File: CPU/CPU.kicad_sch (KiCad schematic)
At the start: 219 parts, among them J1 Conn_02x36_Top_Bottom, P2 Conn_02x13_Top_Bottom, P3 Conn_02x13_Top_Bottom, P4 IDC-16, P5 Conn_02x25_Counter_Clockwise, P6 Conn_02x25_Counter_Clockwise, P7 Conn_02x07_Counter_Clockwise, P8 Conn_02x08_Odd_Even

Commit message: CPU: Fix a huuuge erratum
CPU-E001: AMD SRAM chips use wide footprints (10.16 mm); a standard 7.62mm
width was errorneously used instead

This allows to slightly improve power layout by adding a couple more thick
tracks.
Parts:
- U_B10, U_B9: footprint Package_DIP:DIP-22_W7.62mm_Socket -> Package_DIP:DIP-22_W10.16mm_Socket
- U_D14, U_D15: footprint Package_DIP:DIP-22_W7.62mm_Socket -> Package_DIP:DIP-22_W10.16mm
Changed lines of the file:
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@@
       (effects (font (size 1.27 1.27)) (justify left))
     )
-    (property "Footprint" "Package_DIP:DIP-22_W7.62mm_Socket" (id 2) (at 215.9 374.65 0)
+    (property "Footprint" "Package_DIP:DIP-22_W10.16mm_Socket" (id 2) (at 215.9 374.65 0)
       (effects (font (size 1.27 1.27)) hide)
     )
@@
       (effects (font (size 1.27 1.27)) (justify left))
     )
-    (property "Footprint" "Package_DIP:DIP-22_W7.62mm_Socket" (id 2) (at 215.9 295.91 0)
+    (property "Footprint" "Package_DIP:DIP-22_W10.16mm_Socket" (id 2) (at 215.9 295.91 0)
       (effects (font (size 1.27 1.27)) hide)
     )
@@
     )
     (property "Value" "AM93L422" (id 1) (at 429.26 71.12 90))
-    (property "Footprint" "Package_DIP:DIP-22_W7.62mm_Socket" (id 2) (at 429.26 64.77 0)
+    (property "Footprint" "Package_DIP:DIP-22_W10.16mm" (id 2) (at 429.26 64.77 0)
       (effects (font (size 1.27 1.27)) hide)
     )
@@
     )
     (property "Value" "AM93L422" (id 1) (at 429.26 127 90))
-    (property "Footprint" "Package_DIP:DIP-22_W7.62mm_Socket" (id 2) (at 429.26 120.65 0)
+    (property "Footprint" "Package_DIP:DIP-22_W10.16mm" (id 2) (at 429.26 120.65 0)
       (effects (font (size 1.27 1.27)) hide)
     )
@@
     )
     (path "/45380ac4-2d14-4c77-84c9-3c84e236c620"
-      (reference "U_B9") (unit 1) (value "AM93L422") (footprint "Package_DIP:DIP-22_W7.62mm_Socket")
+      (reference "U_B9") (unit 1) (value "AM93L422") (footprint "Package_DIP:DIP-22_W10.16mm_Socket")
     )
     (path "/6deb5b2a-7379-4330-8bd2-28724b38ec03"
-      (reference "U_B10") (unit 1) (value "AM93L422") (footprint "Package_DIP:DIP-22_W7.62mm_Socket")
+      (reference "U_B10") (unit 1) (value "AM93L422") (footprint "Package_DIP:DIP-22_W10.16mm_Socket")
     )
     (path "/0703fd9f-471a-4a41-a6d5-5e01d4106c25"
@@
     )
     (path "/deee1c09-0c5e-4db0-ab39-5f4e3eafb3e0"
-      (reference "U_D14") (unit 1) (value "AM93L422") (footprint "Package_DIP:DIP-22_W7.62mm_Socket")
+      (reference "U_D14") (unit 1) (value "AM93L422") (footprint "Package_DIP:DIP-22_W10.16mm")
     )
     (path "/acd28f59-548b-4a07-82ee-d1004be02013"
-      (reference "U_D15") (unit 1) (value "AM93L422") (footprint "Package_DIP:DIP-22_W7.62mm_Socket")
+      (reference "U_D15") (unit 1) (value "AM93L422") (footprint "Package_DIP:DIP-22_W10.16mm")
     )
     (path "/55c9bb19-11cb-4bdb-80a7-6ae411c5608c"

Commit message: CPU: Fold back resistor arrays
Get rid of lonely termination resistors; now only arrays of 4 and 8 are used.
These should be more widespread.
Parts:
- removed R22: 220, Resistor_THT:R_Axial_DIN0204_L3.6mm_D1.6mm_P5.08mm_Horizontal, symbol Device:R
- removed R23: 330, Resistor_THT:R_Axial_DIN0204_L3.6mm_D1.6mm_P5.08mm_Horizontal, symbol Device:R
- removed R24, R26: 220, Resistor_THT:R_Axial_DIN0204_L3.6mm_D1.6mm_P2.54mm_Vertical, symbol Device:R
- removed R25, R27: 330, Resistor_THT:R_Axial_DIN0204_L3.6mm_D1.6mm_P2.54mm_Vertical, symbol Device:R
- removed R28: 220, Resistor_THT:R_Axial_DIN0204_L3.6mm_D1.6mm_P7.62mm_Horizontal, symbol Device:R
- removed R29: 330, Resistor_THT:R_Axial_DIN0204_L3.6mm_D1.6mm_P7.62mm_Horizontal, symbol Device:R
- removed RN20: 220, Resistor_THT:R_Array_SIP5, symbol Device:R_Network04
- removed RN21: 330, Resistor_THT:R_Array_SIP5, symbol Device:R_Network04
- removed RN24: 330, Resistor_THT:R_Array_SIP4, symbol Device:R_Network03
- removed RN25: 220, Resistor_THT:R_Array_SIP4, symbol Device:R_Network03
- added RN20: 220, Resistor_THT:R_Array_SIP9, symbol Device:R_Network08
- added RN21: 330, Resistor_THT:R_Array_SIP9, symbol Device:R_Network08
- added RN24: 220, Resistor_THT:R_Array_SIP5, symbol Device:R_Network04
- added RN25: 330, Resistor_THT:R_Array_SIP5, symbol Device:R_Network04
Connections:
- net +5V: now also RN20.1 (common), RN24.1 (common)
- net FP.RTI: now also RN24.2 (R1), RN25.2 (R1)
- net GND: now also RN21.1 (common), RN25.1 (common)
- net SW_2: now also RN24.4 (R3), RN25.4 (R3)
- net Sys.~{DRDY}: now also RN20.3 (R2), RN21.3 (R2)
- net Sys.~{INR0}: now also RN20.6 (R5), RN21.6 (R5)
- net Sys.~{INR1}: now also RN20.9 (R8), RN21.9 (R8)
- net Sys.~{INR2}: now also RN20.8 (R7), RN21.8 (R7)
- net Sys.~{INR3}: now also RN20.7 (R6), RN21.7 (R6)
- net Sys.~{INTREQ}: now also RN20.5 (R4), RN21.5 (R4)
- net Sys.~{MemFault}: now also RN20.4 (R3), RN21.4 (R3)
- net ~{ResetFlag}: now also RN24.3 (R2), RN25.3 (R2)
- net at P3.4 (Pin_4), U_L14.12, U_L14.13: now also RN24.5 (R4), RN25.5 (R4)
- no-connect marks 93 -> 94

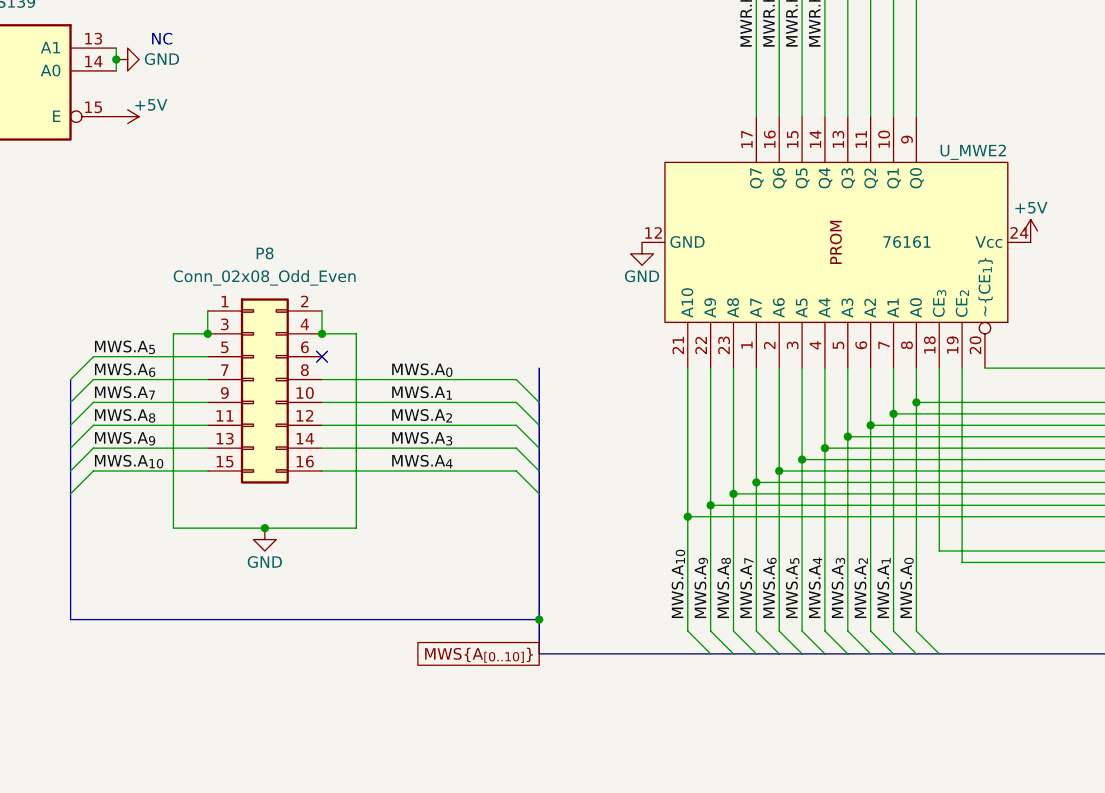
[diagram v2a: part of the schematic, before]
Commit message: CPU: Improve uROM debugging
Bring back uROM disable on P8 pin 6. This may be handy for testing the board.
Also provide +5V on the connector. During debugging we may want to force 1 on
certain MW lines, so +5V on the debug connector may be handy for that.
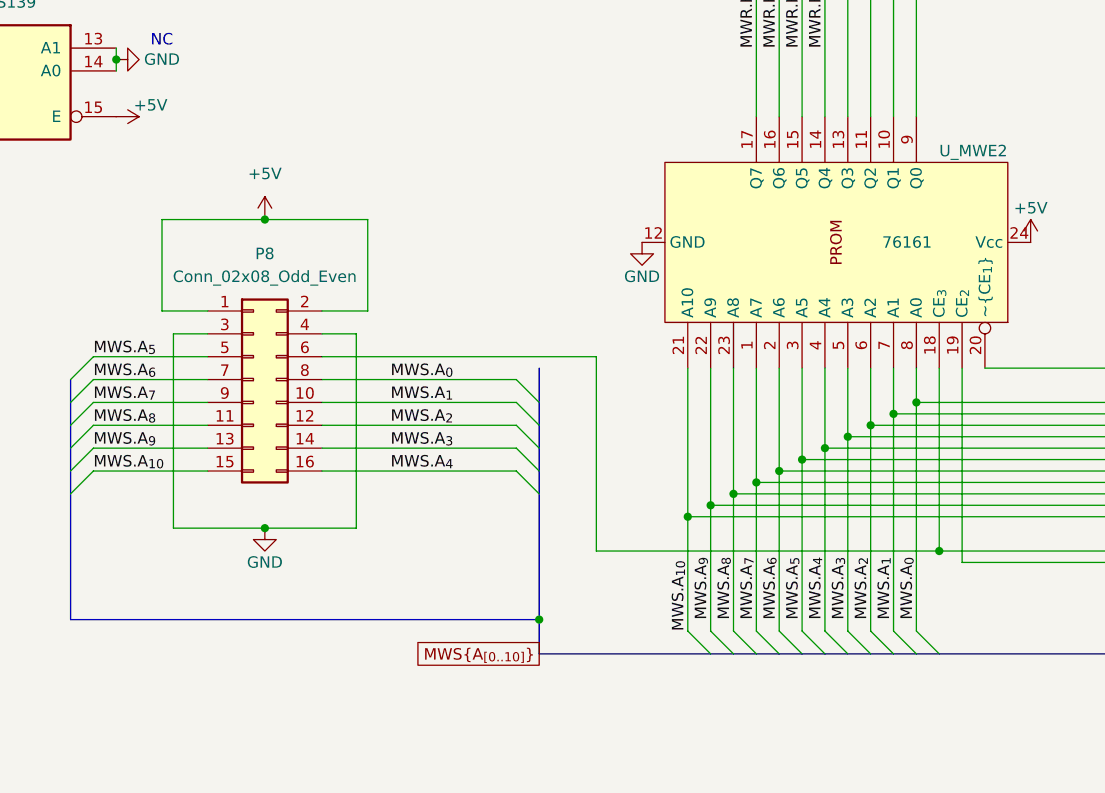
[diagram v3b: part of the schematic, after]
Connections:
- net +5V: now also P8.1 (Pin_1), P8.2 (Pin_2)
- net GND: no longer P8.1 (Pin_1), P8.2 (Pin_2)
- net at R11.2, U_MWE2.18 (CE_{3}), U_MWF2.18 (CE_{3})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: now also P8.6 (Pin_6)
- no-connect marks 94 -> 93
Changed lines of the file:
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@@
   (junction (at 330.2 381) (diameter 0) (color 0 0 0 0)
   )
-  (junction (at 427.99 744.22) (diameter 0) (color 0 0 0 0)
-  )
   (junction (at 669.29 337.82) (diameter 0) (color 0 0 0 0)
   )
@@
   (junction (at 229.87 749.3) (diameter 0) (color 0 0 0 0)
   )
+  (junction (at 509.27 768.35) (diameter 0) (color 0 0 0 0)
+  )
   (junction (at 732.79 760.73) (diameter 0) (color 0 0 0 0)
   )
@@
   (junction (at 901.7 54.61) (diameter 0) (color 0 0 0 0)
   )
-  (junction (at 440.69 744.22) (diameter 0) (color 0 0 0 0)
-  )
   (junction (at 636.27 139.7) (diameter 0) (color 0 0 0 0)
   )
@@
   (junction (at 1066.8 685.8) (diameter 0) (color 0 0 0 0)
   )
+  (junction (at 434.34 731.52) (diameter 0) (color 0 0 0 0)
+  )
   (junction (at 935.99 54.61) (diameter 0) (color 0 0 0 0)
   )
@@
   (no_connect (at 334.01 414.02))
   (no_connect (at 334.01 406.4))
-  (no_connect (at 440.69 746.76))
   (no_connect (at 289.56 142.24))
   (no_connect (at 386.08 356.87))
@@
     (stroke (width 0) (type default) (color 189 121 184 1))
   )
+  (wire (pts (xy 471.17 746.76) (xy 471.17 768.35))
+    (stroke (width 0) (type default) (color 0 0 0 0))
+  )
   (wire (pts (xy 848.36 127) (xy 855.98 127))
     (stroke (width 0) (type default) (color 0 0 0 0))
@@
     (stroke (width 0) (type default) (color 0 0 0 0))
   )
+  (wire (pts (xy 422.91 731.52) (xy 422.91 741.68))
+    (stroke (width 0) (type default) (color 0 0 0 0))
+  )
   (wire (pts (xy 509.27 115.57) (xy 523.24 115.57))
     (stroke (width 0) (type default) (color 0 0 0 0))
@@
     (stroke (width 0) (type default) (color 0 0 0 0))
   )
+  (wire (pts (xy 422.91 741.68) (xy 427.99 741.68))
+    (stroke (width 0) (type default) (color 0 0 0 0))
+  )
   (wire (pts (xy 572.77 648.97) (xy 572.77 666.75))
     (stroke (width 0) (type default) (color 0 0 0 0))
@@
     (stroke (width 0) (type default) (color 0 0 0 0))
   )
-  (wire (pts (xy 440.69 741.68) (xy 440.69 744.22))
-    (stroke (width 0) (type default) (color 0 0 0 0))
-  )
   (wire (pts (xy 643.89 692.15) (xy 643.89 679.45))
     (stroke (width 0) (type default) (color 0 0 0 0))
@@
     (stroke (width 0) (type default) (color 0 0 0 0))
   )
+  (wire (pts (xy 471.17 768.35) (xy 509.27 768.35))
+    (stroke (width 0) (type default) (color 0 0 0 0))
+  )
   (wire (pts (xy 825.5 466.09) (xy 820.42 466.09))
     (stroke (width 0) (type default) (color 0 0 0 0))
@@
     (stroke (width 0) (type default) (color 0 0 0 0))
   )
+  (wire (pts (xy 440.69 741.68) (xy 445.77 741.68))
+    (stroke (width 0) (type default) (color 0 0 0 0))
+  )
   (wire (pts (xy 551.18 480.06) (xy 570.23 480.06))
     (stroke (width 0) (type default) (color 0 0 0 0))
@@
     (stroke (width 0) (type default) (color 0 0 0 0))
   )
-  (wire (pts (xy 427.99 741.68) (xy 427.99 744.22))
-    (stroke (width 0) (type default) (color 0 0 0 0))
-  )
   (wire (pts (xy 405.13 78.74) (xy 405.13 121.92))
     (stroke (width 0) (type default) (color 0 0 0 0))
@@
     (stroke (width 0) (type default) (color 0 0 0 0))
   )
+  (wire (pts (xy 445.77 741.68) (xy 445.77 731.52))
+    (stroke (width 0) (type default) (color 0 0 0 0))
+  )
   (wire (pts (xy 1103.63 267.97) (xy 1103.63 265.43))
     (stroke (width 0) (type default) (color 0 0 0 0))
@@
     (stroke (width 0) (type default) (color 0 0 0 0))
   )
+  (wire (pts (xy 440.69 746.76) (xy 471.17 746.76))
+    (stroke (width 0) (type default) (color 0 0 0 0))
+  )
   (wire (pts (xy 855.98 563.88) (xy 855.98 568.96))
     (stroke (width 0) (type default) (color 0 0 0 0))
@@
     (stroke (width 0) (type default) (color 0 0 0 0))
   )
+  (wire (pts (xy 445.77 731.52) (xy 434.34 731.52))
+    (stroke (width 0) (type default) (color 0 0 0 0))
+  )
   (wire (pts (xy 642.62 553.72) (xy 642.62 535.94))
     (stroke (width 0) (type default) (color 0 0 0 0))
@@
     (stroke (width 0) (type default) (color 0 0 0 0))
   )
+  (wire (pts (xy 434.34 731.52) (xy 422.91 731.52))
+    (stroke (width 0) (type default) (color 0 0 0 0))
+  )
   (bus (pts (xy 185.42 304.8) (xy 185.42 307.34))
     (stroke (width 0) (type default) (color 0 0 0 0))
@@
     (effects (font (size 1.27 1.27)) (justify left bottom))
   )
-  (label "MWS.A_{10}" (at 481.33 775.97 90)
+  (label "MWS.A_{10}" (at 481.33 777.24 90)
     (effects (font (size 1.27 1.27)) (justify left bottom))
   )
@@
     (pin "1")
   )
+  (symbol (lib_id "power:+5V") (at 434.34 731.52 0) (unit 1)
+    (in_bom yes) (on_board yes) (fields_autoplaced)
+    (property "Reference" "#PWR?" (id 0) (at 434.34 735.33 0)
+      (effects (font (size 1.27 1.27)) hide)
+    )
+    (property "Value" "+5V" (id 1) (at 434.34 726.44 0))
+    (property "Footprint" "" (id 2) (at 434.34 731.52 0)
+      (effects (font (size 1.27 1.27)) hide)
+    )
+    (property "Datasheet" "" (id 3) (at 434.34 731.52 0)
+      (effects (font (size 1.27 1.27)) hide)
+    )
+    (pin "1")
+  )
   (symbol (lib_id "74xx:74LS02") (at 638.81 127 90) (unit 3)
     (in_bom yes) (on_board yes)
@@
       (reference "#PWR0285") (unit 1) (value "+5V") (footprint "")
     )
+    (path "/383a3a47-54a4-4eda-bdc6-6fa099d35b87"
+      (reference "#PWR?") (unit 1) (value "+5V") (footprint "")
+    )
     (path "/82ce69c1-2705-465b-8811-8f88b7c3daa0"

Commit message: CPU: Fix C3 footprint
Fix broken footprint (forgot to update footprints in the SCH)
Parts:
- C3: footprint Capacitor_THT:C_Rect_L9.0mm_W2.5mm_P7.50mm_MKT -> Capacitor_THT:C_Disc_D4.3mm_W1.9mm_P5.00mm
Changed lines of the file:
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@@
       (effects (font (size 1.27 1.27)) (justify left))
     )
-    (property "Footprint" "Capacitor_THT:C_Rect_L9.0mm_W2.5mm_P7.50mm_MKT" (id 2) (at 1026.16 637.54 0)
+    (property "Footprint" "Capacitor_THT:C_Disc_D4.3mm_W1.9mm_P5.00mm" (id 2) (at 1026.16 637.54 0)
       (effects (font (size 1.27 1.27)) hide)
     )
@@
   (symbol (lib_id "power:+5V") (at 434.34 731.52 0) (unit 1)
     (in_bom yes) (on_board yes) (fields_autoplaced)
-    (property "Reference" "#PWR?" (id 0) (at 434.34 735.33 0)
+    (property "Reference" "#PWR0187" (id 0) (at 434.34 735.33 0)
       (effects (font (size 1.27 1.27)) hide)
     )
@@
       (reference "#PWR0186") (unit 1) (value "+5V") (footprint "")
     )
+    (path "/383a3a47-54a4-4eda-bdc6-6fa099d35b87"
+      (reference "#PWR0187") (unit 1) (value "+5V") (footprint "")
+    )
     (path "/41917ead-eae6-480a-83b8-b494ad5c8dec"
       (reference "#PWR0191") (unit 1) (value "+5V") (footprint "")
@@
       (reference "#PWR0285") (unit 1) (value "+5V") (footprint "")
     )
-    (path "/383a3a47-54a4-4eda-bdc6-6fa099d35b87"
-      (reference "#PWR?") (unit 1) (value "+5V") (footprint "")
-    )
     (path "/82ce69c1-2705-465b-8811-8f88b7c3daa0"
       (reference "C1") (unit 1) (value "100nF") (footprint "Capacitor_THT:C_Disc_D4.3mm_W1.9mm_P5.00mm")
@@
     )
     (path "/0f488a23-ea0e-4780-80ac-4f6e8ac2653f"
-      (reference "C3") (unit 1) (value "100nF") (footprint "Capacitor_THT:C_Rect_L9.0mm_W2.5mm_P7.50mm_MKT")
+      (reference "C3") (unit 1) (value "100nF") (footprint "Capacitor_THT:C_Disc_D4.3mm_W1.9mm_P5.00mm")
     )
     (path "/f5194f1e-b840-46bc-8058-8e146ee9b6db"

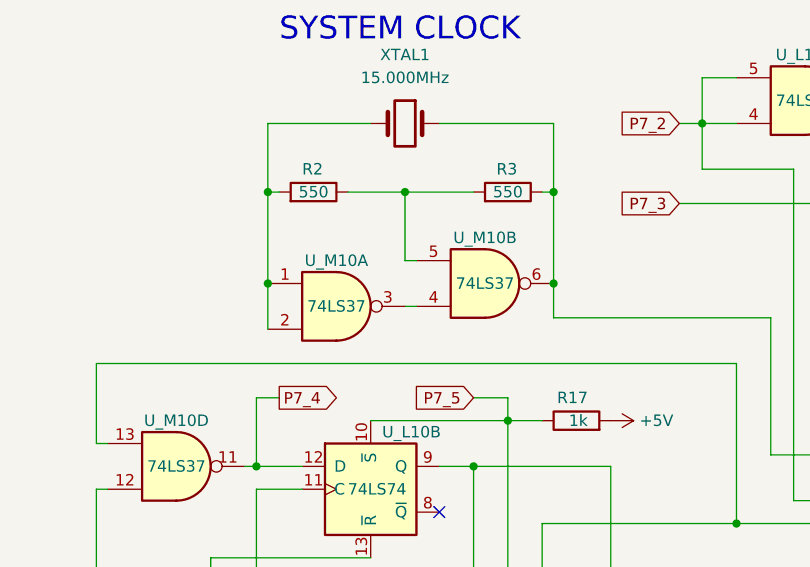
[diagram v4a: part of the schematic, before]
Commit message: CPU: Add missing connection
CPU-E002: Add missing connection between U_M10 pins 4 and 5.
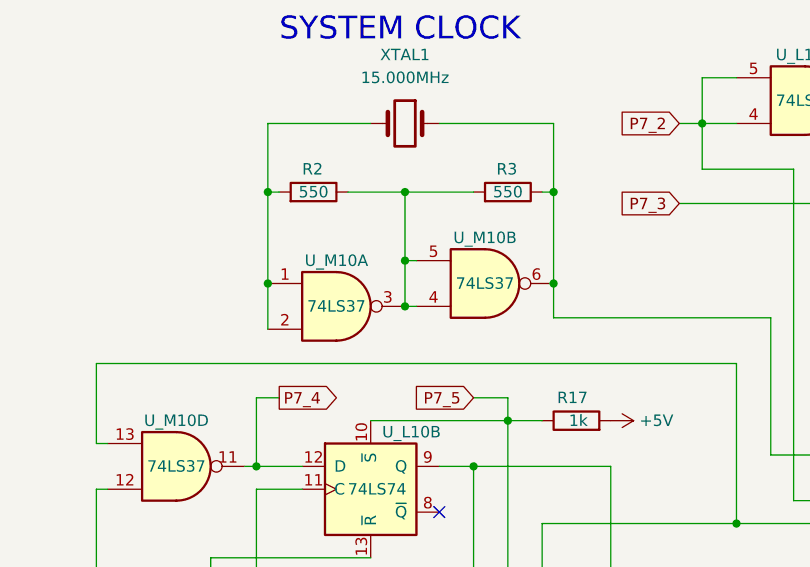
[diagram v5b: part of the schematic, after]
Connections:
- net at U_M10.3, U_M10.4: now also R2.1, R3.2, U_M10.5
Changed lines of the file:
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@@
   (junction (at 58.42 490.22) (diameter 0) (color 0 0 0 0)
   )
+  (junction (at 904.24 326.39) (diameter 0) (color 0 0 0 0)
+  )
   (junction (at 139.7 452.12) (diameter 0) (color 0 0 0 0)
   )
@@
   (junction (at 730.25 762) (diameter 0) (color 0 0 0 0)
   )
+  (junction (at 904.24 321.31) (diameter 0) (color 0 0 0 0)
+  )
   (junction (at 633.73 142.24) (diameter 0) (color 0 0 0 0)
   )
@@
     (stroke (width 0) (type default) (color 0 0 0 0))
   )
+  (wire (pts (xy 904.24 321.31) (xy 904.24 326.39))
+    (stroke (width 0) (type default) (color 0 0 0 0))
+  )

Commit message: CPU: Sync footprints
Update footprint assignment from the PCB
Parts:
- C9: footprint Capacitor_THT:C_Rect_L9.0mm_W2.5mm_P7.50mm_MKT -> Capacitor_THT:C_Disc_D4.3mm_W1.9mm_P5.00mm
- R17: footprint Resistor_THT:R_Axial_DIN0204_L3.6mm_D1.6mm_P5.08mm_Horizontal -> Resistor_THT:R_Axial_DIN0204_L3.6mm_D1.6mm_P7.62mm_Horizontal
- R18: footprint Resistor_THT:R_Axial_DIN0207_L6.3mm_D2.5mm_P7.62mm_Horizontal -> Resistor_THT:R_Axial_DIN0207_L6.3mm_D2.5mm_P10.16mm_Horizontal
- XTAL1: footprint Crystal:Crystal_HC18-U_Vertical -> Crystal:Crystal_HC49-U_Horizontal
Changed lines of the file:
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@@
     (property "Reference" "XTAL1" (id 0) (at 904.24 298.45 0))
     (property "Value" "15.000MHz" (id 1) (at 904.24 300.99 0))
-    (property "Footprint" "Crystal:Crystal_HC18-U_Vertical" (id 2) (at 904.24 306.07 0)
+    (property "Footprint" "Crystal:Crystal_HC49-U_Horizontal" (id 2) (at 904.24 306.07 0)
       (effects (font (size 1.27 1.27)) hide)
     )
@@
     (property "Reference" "R18" (id 0) (at 257.81 457.2 90))
     (property "Value" "4.7k" (id 1) (at 257.81 459.74 90))
-    (property "Footprint" "Resistor_THT:R_Axial_DIN0207_L6.3mm_D2.5mm_P7.62mm_Horizontal" (id 2) (at 257.81 461.518 90)
+    (property "Footprint" "Resistor_THT:R_Axial_DIN0207_L6.3mm_D2.5mm_P10.16mm_Horizontal" (id 2) (at 257.81 461.518 90)
       (effects (font (size 1.27 1.27)) hide)
     )
@@
       (effects (font (size 1.27 1.27)) (justify left))
     )
-    (property "Footprint" "Capacitor_THT:C_Rect_L9.0mm_W2.5mm_P7.50mm_MKT" (id 2) (at 1094.74 637.54 0)
+    (property "Footprint" "Capacitor_THT:C_Disc_D4.3mm_W1.9mm_P5.00mm" (id 2) (at 1094.74 637.54 0)
       (effects (font (size 1.27 1.27)) hide)
     )
@@
       (effects (font (size 1.27 1.27)) (justify left))
     )
-    (property "Footprint" "Resistor_THT:R_Axial_DIN0204_L3.6mm_D1.6mm_P5.08mm_Horizontal" (id 2) (at 923.29 340.868 90)
+    (property "Footprint" "Resistor_THT:R_Axial_DIN0204_L3.6mm_D1.6mm_P7.62mm_Horizontal" (id 2) (at 923.29 340.868 90)
       (effects (font (size 1.27 1.27)) hide)
     )
@@
     )
     (path "/cb5edacb-cef0-48ec-b566-49dafe933ca0"
-      (reference "C9") (unit 1) (value "100nF") (footprint "Capacitor_THT:C_Rect_L9.0mm_W2.5mm_P7.50mm_MKT")
+      (reference "C9") (unit 1) (value "100nF") (footprint "Capacitor_THT:C_Disc_D4.3mm_W1.9mm_P5.00mm")
     )
     (path "/15144e0d-74c4-4070-8b3c-203df6509857"
@@
     )
     (path "/ea02ea21-72eb-4d2a-a89e-9df0175404a8"
-      (reference "R17") (unit 1) (value "1k") (footprint "Resistor_THT:R_Axial_DIN0204_L3.6mm_D1.6mm_P5.08mm_Horizontal")
+      (reference "R17") (unit 1) (value "1k") (footprint "Resistor_THT:R_Axial_DIN0204_L3.6mm_D1.6mm_P7.62mm_Horizontal")
     )
     (path "/b952ec4b-ff73-4a94-99ed-943280ef2677"
-      (reference "R18") (unit 1) (value "4.7k") (footprint "Resistor_THT:R_Axial_DIN0207_L6.3mm_D2.5mm_P7.62mm_Horizontal")
+      (reference "R18") (unit 1) (value "4.7k") (footprint "Resistor_THT:R_Axial_DIN0207_L6.3mm_D2.5mm_P10.16mm_Horizontal")
     )
     (path "/2a1ee668-14d7-4c32-86e1-1aefa86759e0"
@@
     )
     (path "/062033f7-deb0-4cd0-a29c-ab8812e00794"
-      (reference "XTAL1") (unit 1) (value "15.000MHz") (footprint "Crystal:Crystal_HC18-U_Vertical")
+      (reference "XTAL1") (unit 1) (value "15.000MHz") (footprint "Crystal:Crystal_HC49-U_Horizontal")
     )
   )
